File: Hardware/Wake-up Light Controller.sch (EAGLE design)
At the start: 37 parts, among them IC1 ST1S10, IC2 HT7333, IC3 DS3231/SO, IC4 ATMEGA328P_TQFP, J1 AVR-ISP-6PIN, Q1 BSS138, Q2 BSS138, Q3 FDN306P, Q4 FDD8447L, U1 HC_05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

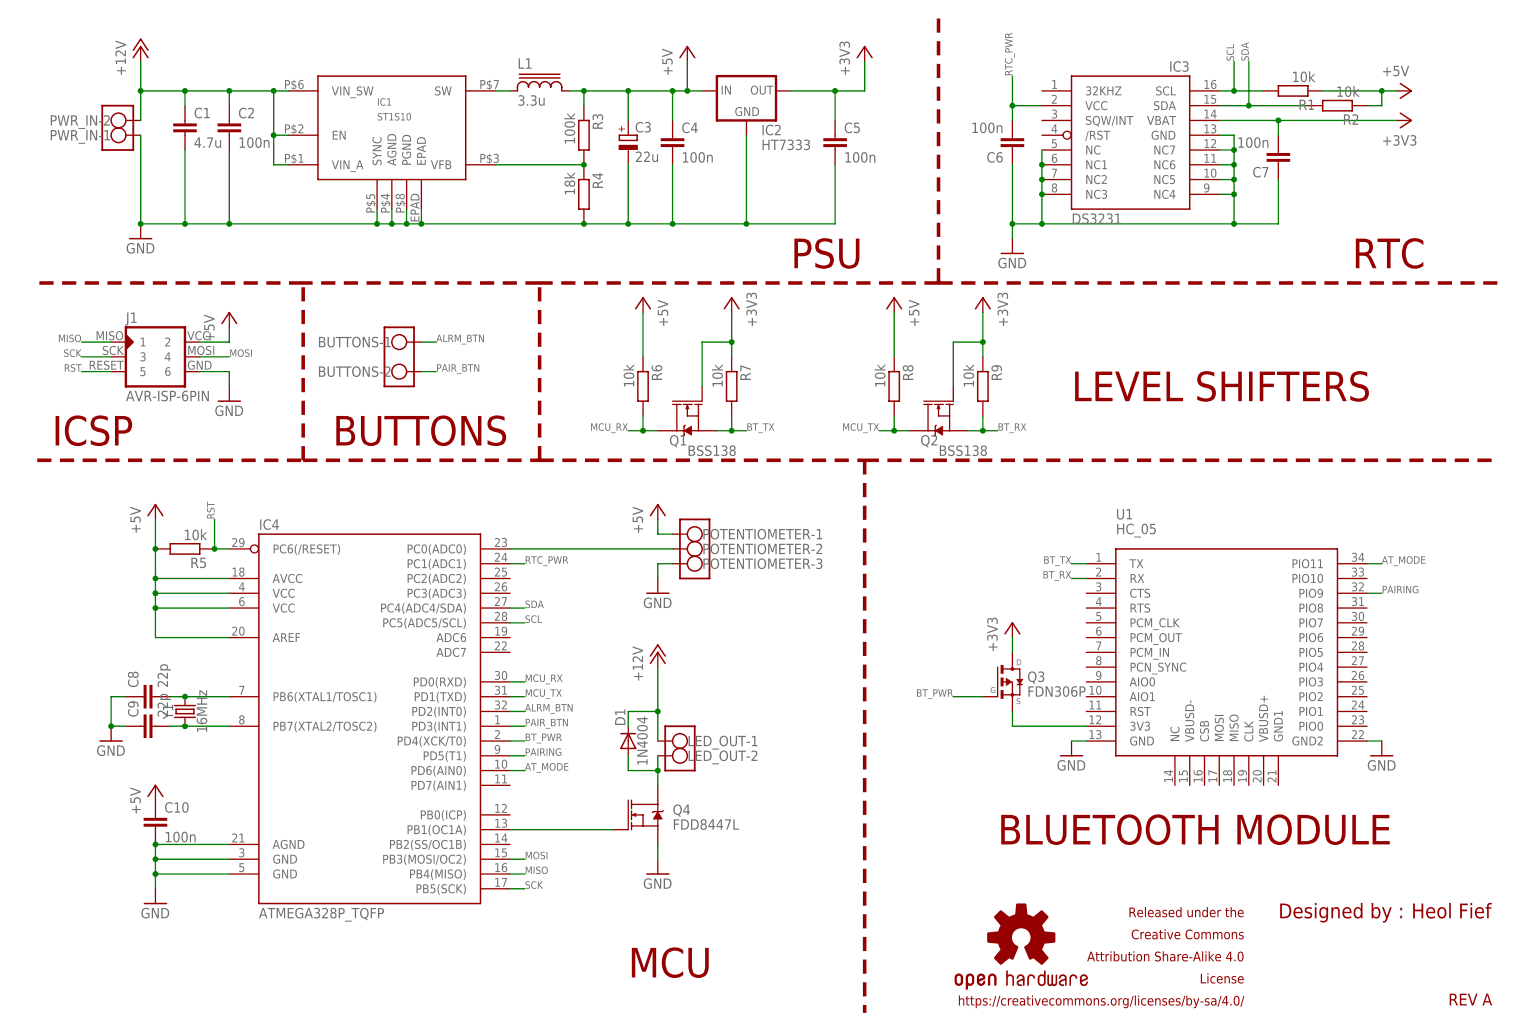
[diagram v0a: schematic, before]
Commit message: Place silkscreen
Place silkscreen, and change i2c pullups to 4.7k ohm
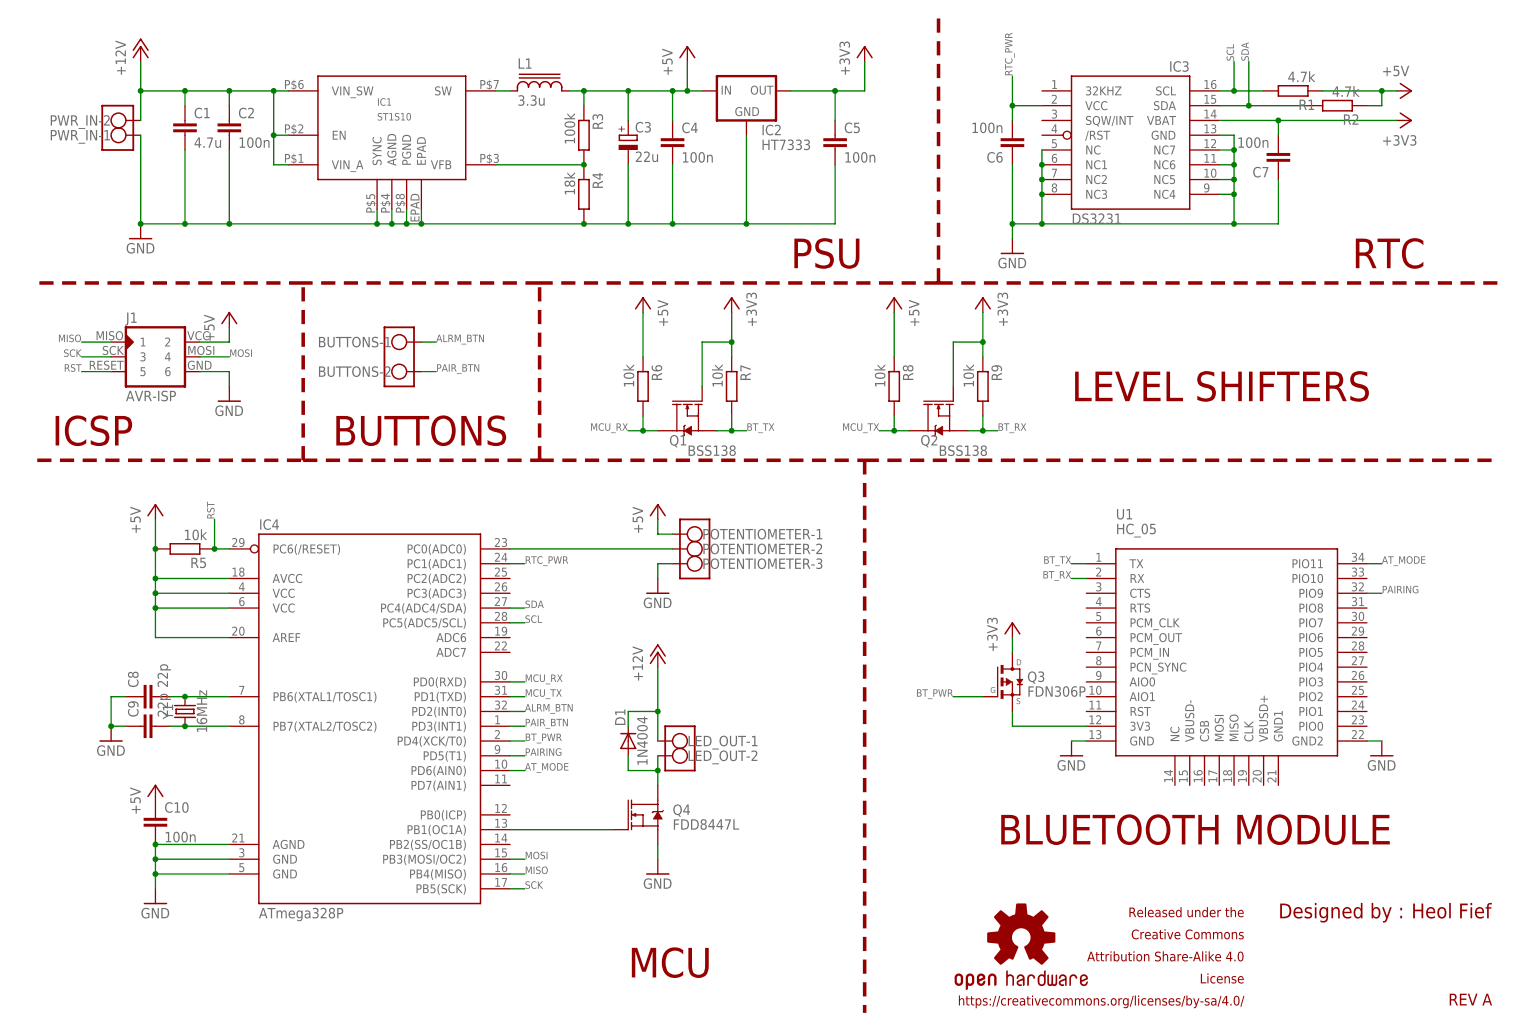
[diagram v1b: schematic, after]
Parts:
- IC4: value ATMEGA328P_TQFP -> ATmega328P
- J1: value AVR-ISP-6PIN -> AVR-ISP
- R1, R2: value 10k -> 4.7k
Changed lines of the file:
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@@
 </classes>
 <parts>
-<part name="IC4" library="SparkFun-IC-Microcontroller" deviceset="ATMEGA328P_TQFP" device="" value="ATMEGA328P_TQFP"/>
+<part name="IC4" library="SparkFun-IC-Microcontroller" deviceset="ATMEGA328P_TQFP" device="" value="ATmega328P"/>
 <part name="GND9" library="supply1" deviceset="GND" device=""/>
 <part name="IC3" library="adafruit" deviceset="DS3231" device="/SO"/>
@@
 <part name="C8" library="rcl" deviceset="C-EU" device="C0805" value="22p"/>
 <part name="GND5" library="supply1" deviceset="GND" device=""/>
-<part name="R1" library="resistor" library_urn="urn:adsk.eagle:library:348" deviceset="R-EU_" device="M0805" package3d_urn="urn:adsk.eagle:package:26079/1" value="10k"/>
-<part name="R2" library="resistor" library_urn="urn:adsk.eagle:library:348" deviceset="R-EU_" device="M0805" package3d_urn="urn:adsk.eagle:package:26079/1" value="10k"/>
+<part name="R1" library="resistor" library_urn="urn:adsk.eagle:library:348" deviceset="R-EU_" device="M0805" package3d_urn="urn:adsk.eagle:package:26079/1" value="4.7k"/>
+<part name="R2" library="resistor" library_urn="urn:adsk.eagle:library:348" deviceset="R-EU_" device="M0805" package3d_urn="urn:adsk.eagle:package:26079/1" value="4.7k"/>
 <part name="C7" library="rcl" deviceset="C-EU" device="C0805" value="100n"/>
 <part name="C6" library="rcl" deviceset="C-EU" device="C0805" value="100n"/>
@@
 <part name="GND1" library="supply1" deviceset="GND" device=""/>
 <part name="P+1" library="supply1" deviceset="+12V" device=""/>
-<part name="J1" library="avr-isp" deviceset="AVR-ISP-6PIN" device="AVR-ISP-6PIN-SMALL-SILK" value="AVR-ISP-6PIN"/>
+<part name="J1" library="avr-isp" deviceset="AVR-ISP-6PIN" device="AVR-ISP-6PIN-SMALL-SILK" value="AVR-ISP"/>
 <part name="GND3" library="supply1" deviceset="GND" device=""/>
 <part name="IC2" library="holtek2" deviceset="HT73*" device="" technology="33"/>

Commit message: REV B
Add debug function,
Add RTC battery,
Changed global layout
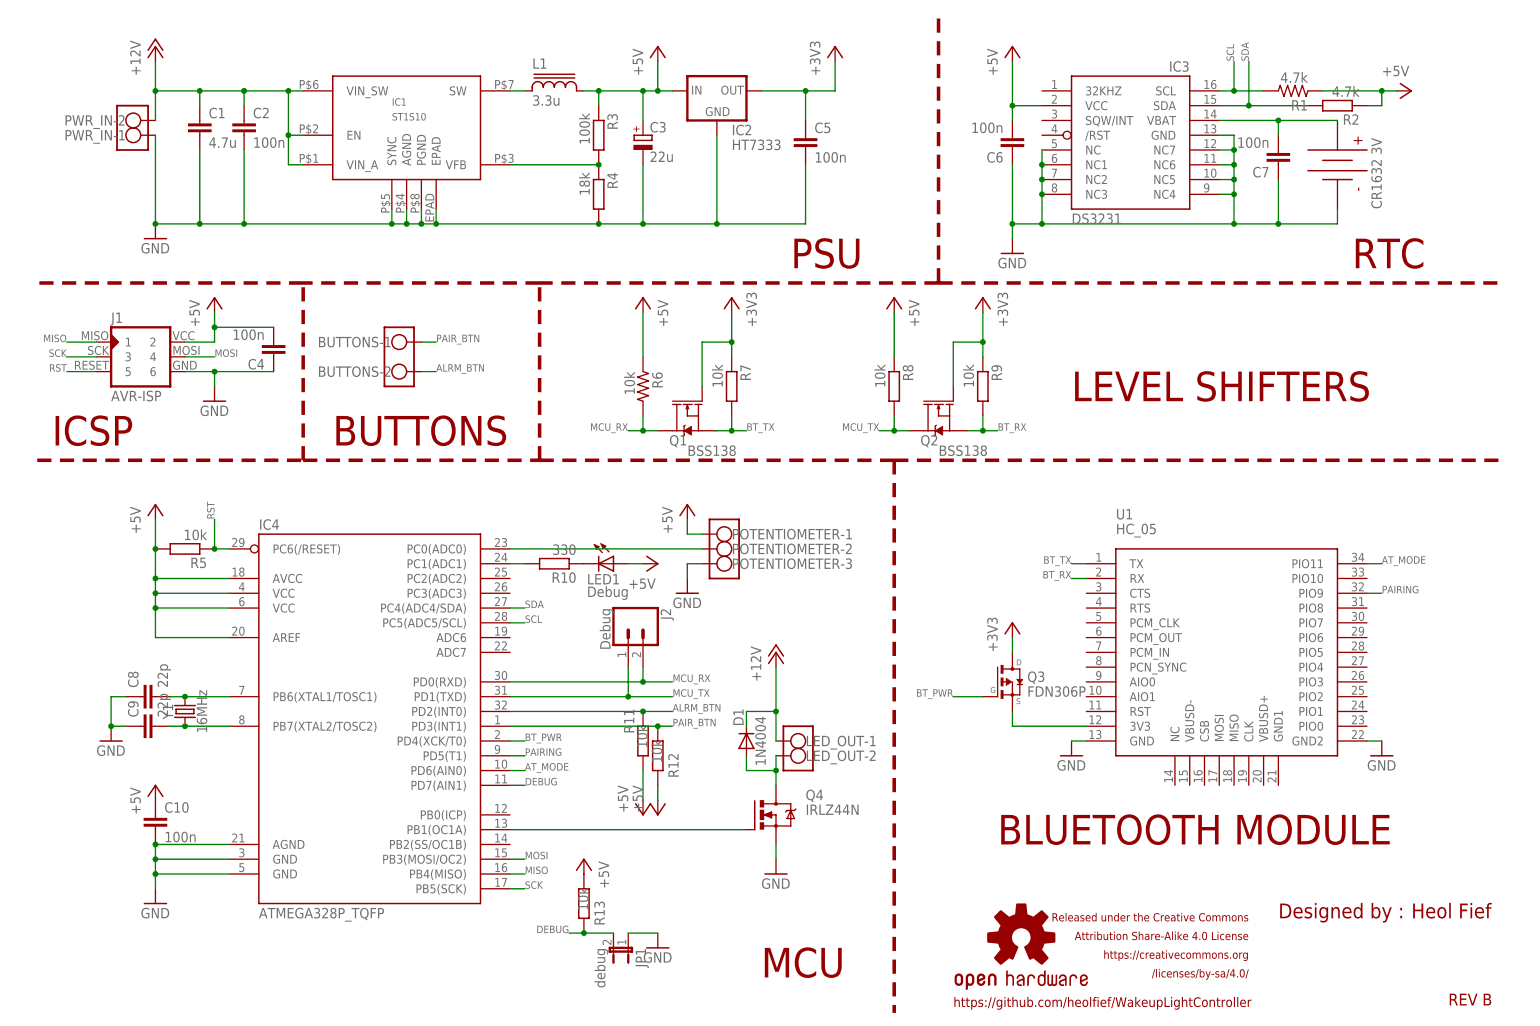
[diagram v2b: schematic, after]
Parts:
- added J2: Debug, SparkFun-Connectors:CONN_021X02_NO_SILK
- added JP1: debug, jumper:JP1E
- added LED1: Debug, led:LEDCHIPLED_0805
- added R10: 330, resistor:R-EU_M0805
- added R11, R12, R13: 10k, resistor:R-EU_M0805
- added U$1: CR1632_3V, heol:BATTCON_16MM_PTH
- IC4: value ATmega328P -> ATMEGA328P_TQFP
- Q4: value FDD8447L -> IRLZ44N; device SparkFun-DiscreteSemi:MOSFET-NCH-FDD8780 -> transistor-power:IRLZ44Z
- R1, R6: device resistor:R-EU_M0805 -> rc-master-smd:R_0805MP
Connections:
- removed net RTC_PWR: C6.2, IC3.VCC, IC4.PC1(ADC1)
- new net DEBUG: IC4.PD7(AIN1), JP1.2, R13.1
- new net N$3: IC4.PC1(ADC1), R10.2
- new net N$8: LED1.C, R10.1
- new net VBAT: C7.2, IC3.VBAT, U$1.VCC
- net +3V3: no longer C7.2, IC3.VBAT
- net +5V: now also C4.2, C6.2, IC3.VCC, LED1.A, R11.1, R12.1, R13.2; no longer C4.1
- net ALRM_BTN: now also BUTTONS-2.KL, R11.2; no longer BUTTONS-1.KL
- net GND: now also C4.1, JP1.1, U$1.GND; no longer C4.2
- net MCU_RX: now also J2.2
- net MCU_TX: now also J2.1
- net PAIR_BTN: now also BUTTONS-1.KL, R12.2; no longer BUTTONS-2.KL
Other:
- note added: "CR1632 3V"
- note added: "REV B"
- note added: "Released under the Creative Commons Attribution Share-Alike 4.0 License https://creativecommons.org /licenses/by-sa/4.0/"
- note added: "https://github.com/heolfief/WakeupLightController"
- note removed: "REV A"
- note removed: "Released under the Creative Commons Attribution Share-Alike 4.0 License https://creativecommons.org/licenses/by-sa/4.0/"
- moved on the sheet: C1, C2, C3, C4, C5, D1, IC1, IC2, J1, L1, LED_OUT-1, LED_OUT-2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

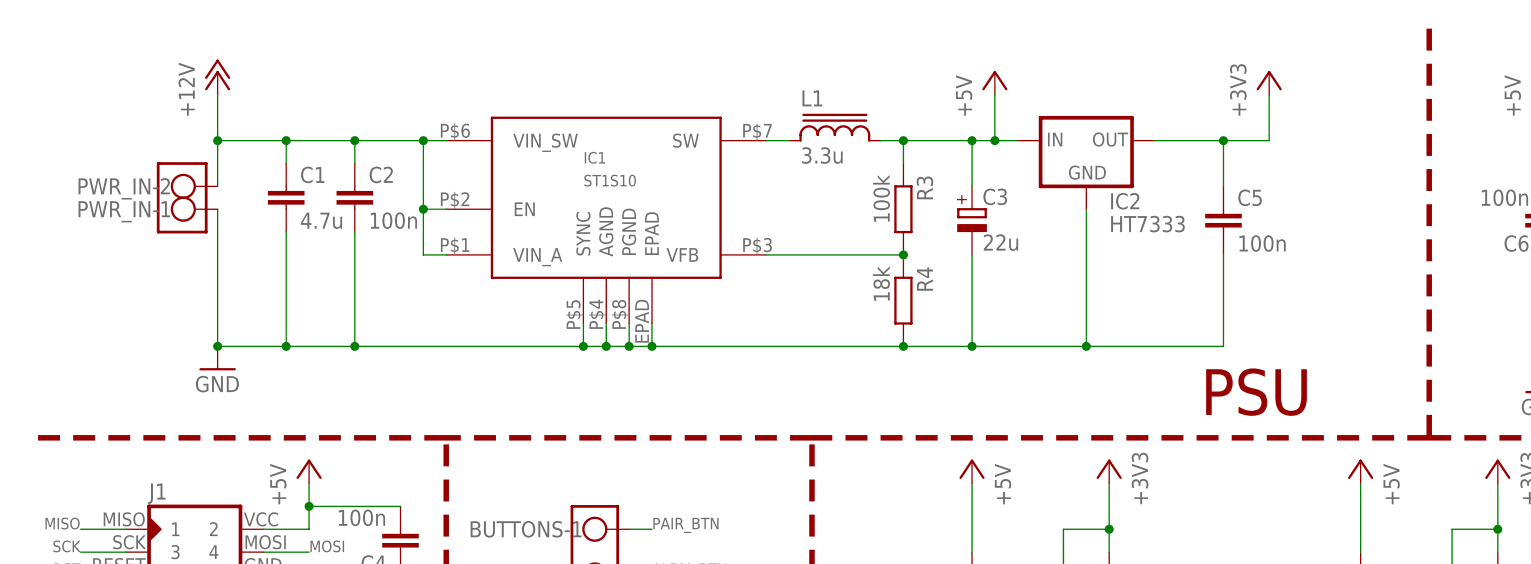
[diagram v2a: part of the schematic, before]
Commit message: Add PTC fuse on 12V input
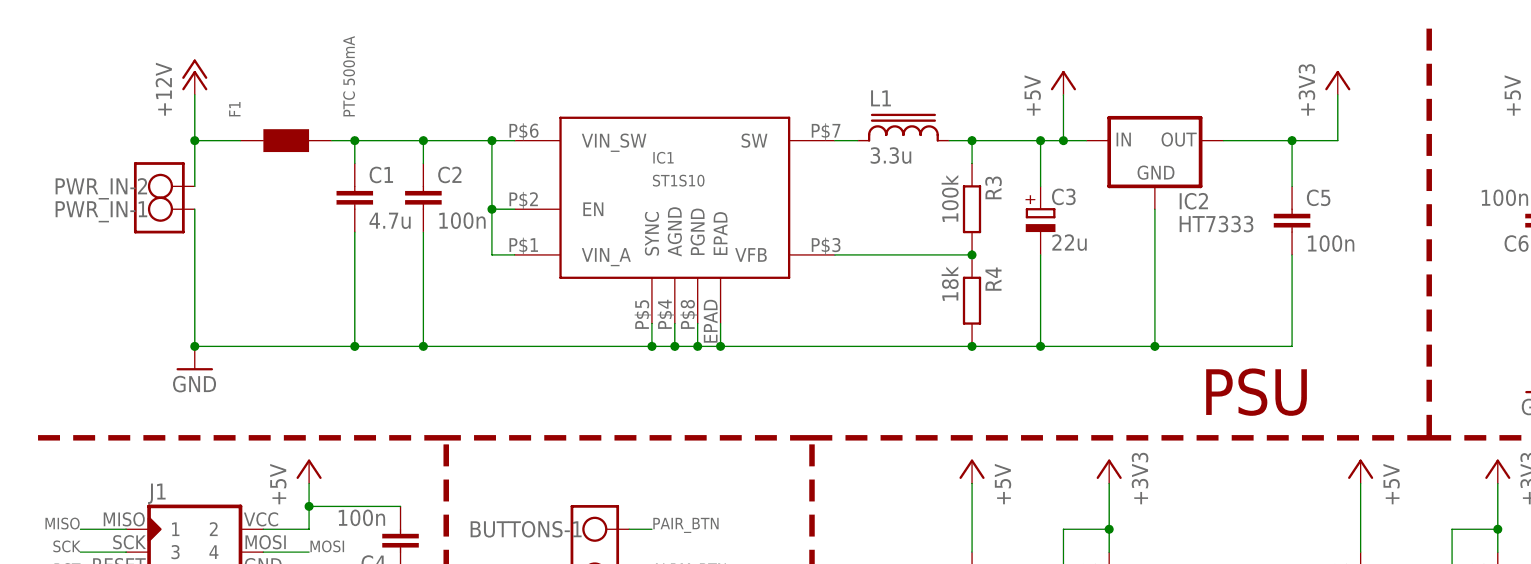
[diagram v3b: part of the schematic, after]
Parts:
- added F1: PTC 500mA, BaseApp:PTC-0.2A-IH/0.5A-IT/40A-IM
- LED1: device led:LEDCHIPLED_0805 -> led:LEDCHIPLED_1206
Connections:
- new net N$9: C1.1, C2.1, F1.2, IC1.EN, IC1.VIN_A, IC1.VIN_SW
- net +12V: now also F1.1; no longer C1.1, C2.1, IC1.EN, IC1.VIN_A, IC1.VIN_SW
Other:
- moved on the sheet: C1, C2, C3, C5, IC1, IC2, L1, PWR_IN-1, PWR_IN-2, R3, R4
